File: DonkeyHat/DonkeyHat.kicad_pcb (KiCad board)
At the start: 2 copper layers, 65 x 56.1 mm, 13 parts, among them J1 GPIO, U1 ProMicro

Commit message: WIP
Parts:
- renumbered OLED1 to OLED, Steering1 to Steering, Throttle1 to Throttle
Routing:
- net +3V3: track 97.3 -> 96.7 mm
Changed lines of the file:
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@@
 		(descr "Through hole straight pin header, 1x03, 2.54mm pitch, single row")
 		(tags "Through hole pin header THT 1x03 2.54mm single row")
-		(property "Reference" "Steering1"
+		(property "Reference" "Steering"
 			(at -2.54 2.54 90)
 			(layer "F.SilkS")
@@
 		(descr "Through hole straight socket strip, 1x04, 2.54mm pitch, single row (from Kicad 4.0.7), script generated")
 		(tags "Through hole socket strip THT 1x04 2.54mm single row")
-		(property "Reference" "OLED1"
+		(property "Reference" "OLED"
 			(at 0 -2.77 0)
 			(layer "F.SilkS")
@@
 		(descr "Through hole straight pin header, 1x03, 2.54mm pitch, single row")
 		(tags "Through hole pin header THT 1x03 2.54mm single row")
-		(property "Reference" "Throttle1"
+		(property "Reference" "Throttle"
 			(at 2.54 2.54 270)
 			(layer "F.SilkS")
@@
 	)
 	(segment
-		(start 104.064 64.948)
-		(end 103.81 65.202)
-		(width 0.2)
-		(layer "B.Cu")
-		(net 6)
-	)
-	(segment
-		(start 103.81 65.202)
-		(end 103.81 69.52)
+		(start 101.778 62.662)
+		(end 103.81 64.694)
 		(width 0.2)
 		(layer "B.Cu")
@@
 	)
 	(segment
-		(start 101.778 62.662)
-		(end 104.064 64.948)
+		(start 101.778 61.138)
+		(end 101.778 62.662)
 		(width 0.2)
 		(layer "B.Cu")
@@
 	)
 	(segment
-		(start 101.778 61.138)
-		(end 101.778 62.662)
+		(start 103.81 64.694)
+		(end 103.81 69.52)
 		(width 0.2)
 		(layer "B.Cu")
@@
 	)
 	(segment
-		(start 102.413 66.218)
-		(end 101.397 67.234)
-		(width 0.2)
-		(layer "B.Cu")
-		(net 31)
-	)
-	(segment
-		(start 101.397 67.488)
-		(end 102.159 68.25)
+		(start 102.159 66.472)
+		(end 102.159 86.03)
 		(width 0.2)
 		(layer "B.Cu")
@@
 	)
 	(segment
-		(start 101.397 67.234)
-		(end 101.397 67.488)
-		(width 0.2)
-		(layer "B.Cu")
-		(net 31)
-	)
-	(segment
 		(start 102.413 64.821)
 		(end 102.413 66.218)
@@
 	)
 	(segment
-		(start 102.159 68.25)
-		(end 102.159 86.03)
+		(start 102.413 66.218)
+		(end 102.159 66.472)
 		(width 0.2)
 		(layer "B.Cu")

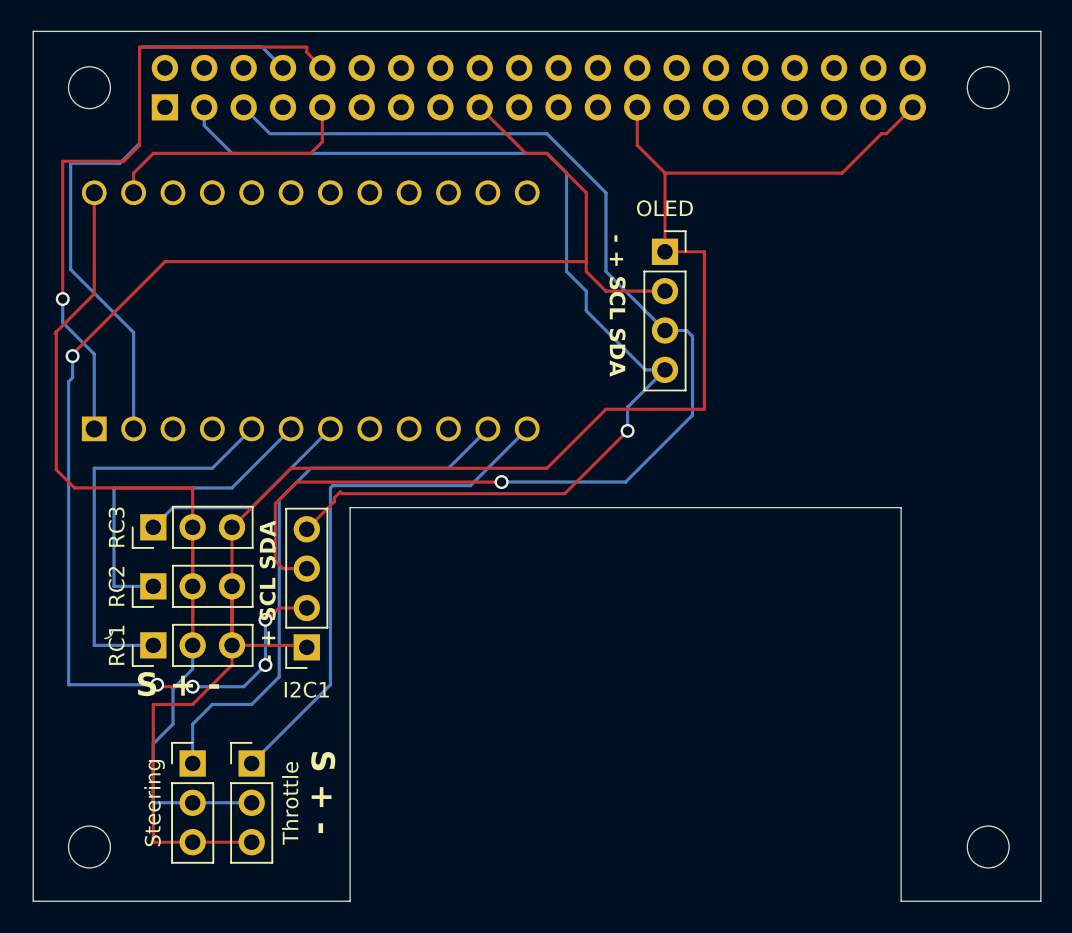
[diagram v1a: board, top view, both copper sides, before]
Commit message: Switched to smaller 2040
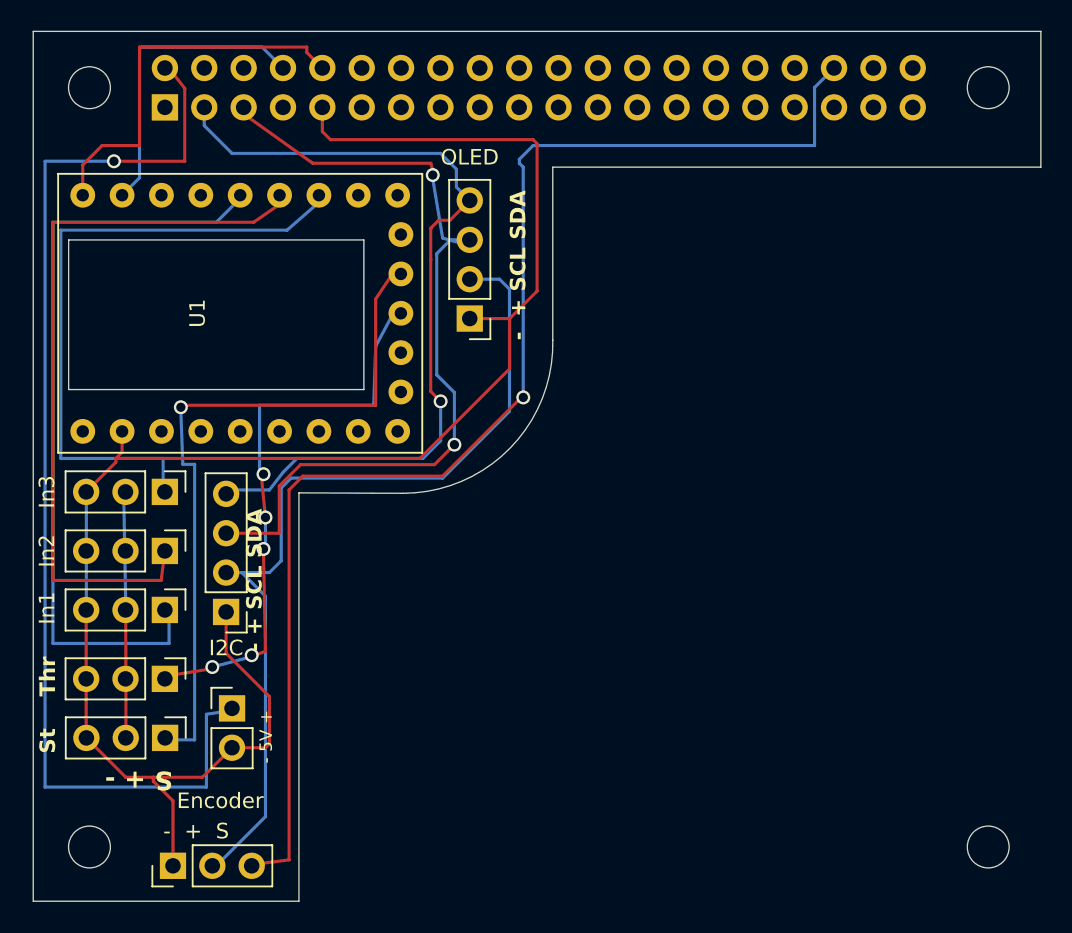
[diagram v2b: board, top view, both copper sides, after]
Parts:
- added Encoder: Conn_01x03_Pin, Connector_PinHeader_2.54mm:PinHeader_1x03_P2.54mm_Vertical, F.Cu at (108.9, 97.7)
- added J2: Conn_01x02_Pin, Connector_PinHeader_2.54mm:PinHeader_1x02_P2.54mm_Vertical, F.Cu at (112.7, 87.6)
- I2C: renamed from I2C1; footprint Connector_PinSocket_2.54mm:PinSocket_1x04_P2.54mm_Vertical -> Connector_PinHeader_2.54mm:PinHeader_1x04_P2.54mm_Vertical
- OLED: footprint Connector_PinSocket_2.54mm:PinSocket_1x04_P2.54mm_Vertical -> Connector_PinHeader_2.54mm:PinHeader_1x04_P2.54mm_Vertical
- U1: footprint promicro:ProMicro-NoSilk -> RP2040-Zero:RP2040-Zero
- moved OLED 13.3 mm to (128.0, 62.4), turned to 180 degrees
- moved U1 11.6 mm to (125.0, 71.1), turned to 90 degrees
- moved Thr1 7.82 mm to (108.4, 85.6), turned to -90 degrees
- moved I2C 5.69 mm to (112.3, 81.3)
- moved St1 2.43 mm to (108.4, 89.5), turned to -90 degrees
- moved In1 2.40 mm to (108.4, 81.2), turned to -90 degrees
- moved In2 2.40 mm to (108.4, 77.4), turned to -90 degrees
- moved In3 2.40 mm to (108.4, 73.6), turned to -90 degrees
- renumbered RC1 to In1, RC2 to In2, RC3 to In3, Steering to St1, Throttle to Thr1
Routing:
- net +BATT: track 62.4 -> 0.02 mm
- net /GPIO3/SCL1: track 78.5 -> 34.2 mm, vias 1 -> 2
- net /GPIO16: track 0.00 -> 40.7 mm, vias 0 -> 1
- net +3V3: track 96.7 -> 57.3 mm, vias 5 -> 0
- net Net-(St1-Pin_1): track 36.2 -> 0.00 mm, vias 0 -> 1
- net Net-(Thr1-Pin_1): track 34.2 -> 0.00 mm, vias 0 -> 5
- net GND: track 132.1 -> 104.4 mm
- net Net-(In1-Pin_1): track 26.5 -> 0.00 mm
- net Net-(In2-Pin_1): track 21.9 -> 0.00 mm
- net /GPIO14/TXD0: track 39.8 -> 19.9 mm
- net /GPIO2/SDA1: track 70.4 -> 51.5 mm
- net /GPIO15/RXD0: track 42.5 -> 25.0 mm, vias 1 -> 0
- net Net-(In3-Pin_1): track 14.1 -> 0.00 mm
- net +5V: vias 0 -> 1
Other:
- outline, holes or cut-outs redrawn
- board text added: "- + S"
- board text added: "- 5V +"
- board text added: "St"
- board text added: "Thr"

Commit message: Added 4-bit encoders
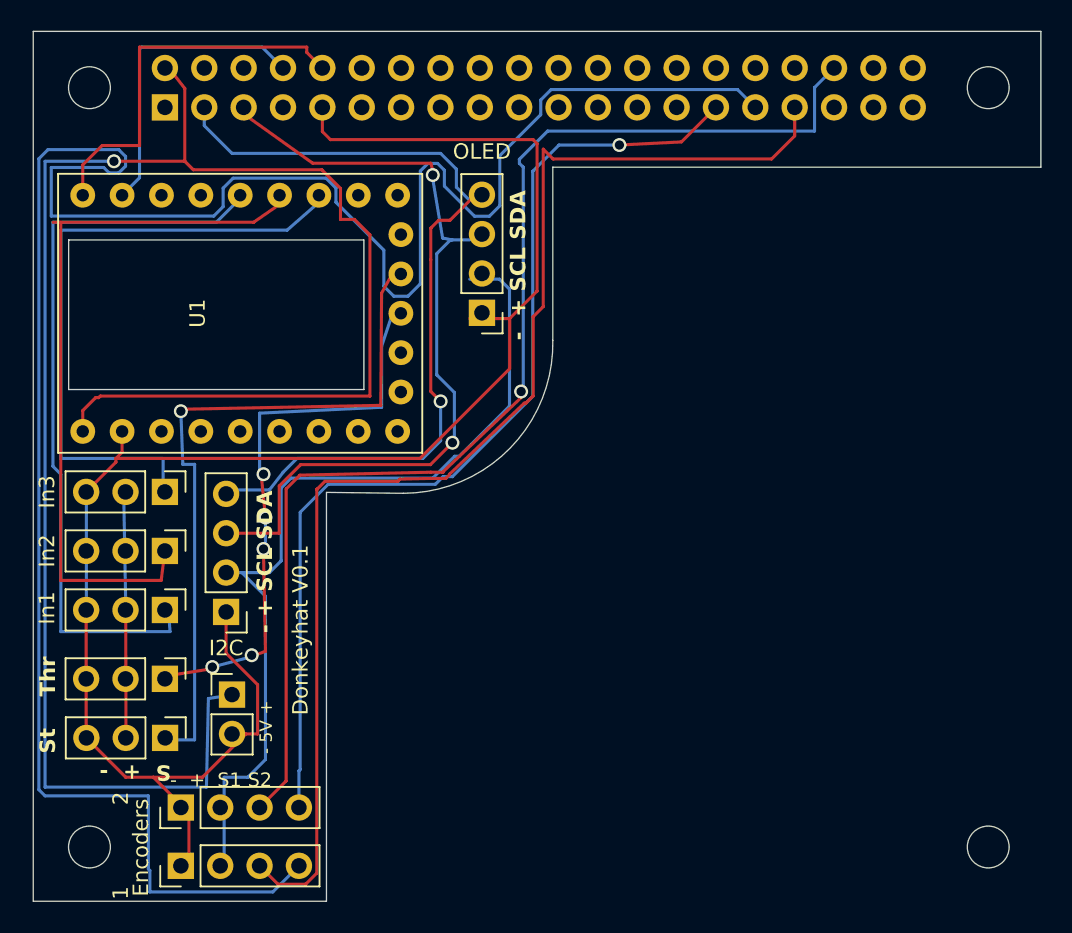
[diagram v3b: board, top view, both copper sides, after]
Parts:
- removed Encoder: Conn_01x03_Pin, Connector_PinHeader_2.54mm:PinHeader_1x03_P2.54mm_Vertical
- added J2: Encoder 2, Connector_PinHeader_2.54mm:PinHeader_1x04_P2.54mm_Vertical, F.Cu at (109.4, 97.7)
- added J3: Encoder 1, Connector_PinHeader_2.54mm:PinHeader_1x04_P2.54mm_Vertical, F.Cu at (109.4, 94.0)
- moved 5V1 0.89 mm to (112.7, 86.7)
- moved OLED 0.87 mm to (128.8, 62.0)
- renumbered J2 to 5V1
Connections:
- U1 pad 22: unconnected-(U1-RST-Pad22) -> +5V
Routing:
- net /GPIO6: track 0.00 -> 147.8 mm
- net /GPIO13/PWM1: track 0.00 -> 80.8 mm
- net /GPIO5: track 0.00 -> 65.4 mm, vias 0 -> 1
- net +5V: track 0.00 -> 45.8 mm
- net /GPIO16: track 40.7 -> 61.8 mm
- net Net-(In1-Pin_1): track 0.00 -> 10.9 mm
- net GND: track 104.4 -> 103.4 mm
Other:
- outline, holes or cut-outs redrawn
- board text added: "- + S1 S2"
- board text added: "1"
- board text added: "2"
- board text added: "Donkeyhat V0.1"
- board text added: "Encoders"
- board text removed: "- + S"

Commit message: Switched encoders to RP2040
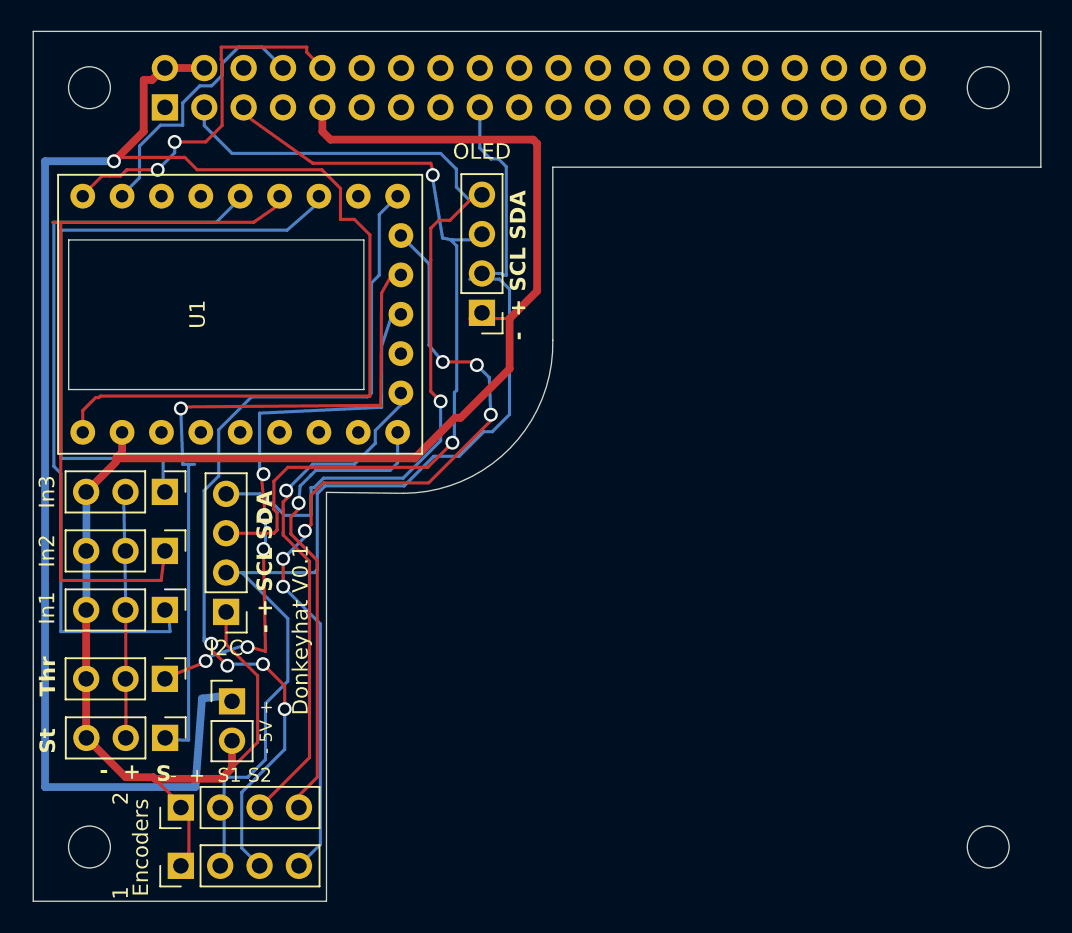
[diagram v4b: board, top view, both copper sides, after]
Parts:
- moved 5V1 0.43 mm to (112.7, 87.1)
- moved U1 0.06 mm to (125.0, 71.1)
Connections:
- J1 pad 31: /GPIO6 -> unconnected-(J1-Pin_31-Pad31)
- J2 pad 3: /GPIO13/PWM1 -> Net-(J2-Pin_3)
- J2 pad 4: /GPIO6 -> Net-(J2-Pin_4)
- J3 pad 3: /GPIO16 -> Net-(J3-Pin_3)
- J3 pad 4: /GPIO5 -> Net-(J3-Pin_4)
- U1 pad 10: unconnected-(U1-E6-Pad10) -> Net-(J2-Pin_4)
- U1 pad 14: unconnected-(U1-B2-Pad14) -> Net-(J3-Pin_3)
- U1 pad 15: unconnected-(U1-B3-Pad15) -> Net-(J3-Pin_4)
- U1 pad 9: unconnected-(U1-D7-Pad9) -> Net-(J2-Pin_3)
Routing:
- net /GPIO6: track 147.8 -> 0.00 mm
- net /GPIO13/PWM1: track 80.8 -> 0.00 mm
- net /GPIO5: track 65.4 -> 0.00 mm, vias 1 -> 0
- net /GPIO16: track 61.8 -> 0.00 mm, vias 1 -> 0
- net Net-(J2-Pin_3): track 0.00 -> 59.1 mm, vias 0 -> 4
- net Net-(J2-Pin_4): track 0.00 -> 56.5 mm, vias 0 -> 6
- net Net-(J3-Pin_3): track 0.00 -> 34.1 mm, vias 0 -> 1
- net Net-(J3-Pin_4): track 0.00 -> 31.2 mm, vias 0 -> 1
- net +3V3: track 57.8 -> 72.9 mm
- net +5V: track 45.8 -> 56.1 mm
- net /GPIO2/SDA1: track 51.5 -> 55.7 mm
- net GND: track 103.4 -> 106.0 mm
- net /GPIO14/TXD0: track 19.9 -> 17.6 mm
- net /GPIO15/RXD0: track 25.0 -> 23.9 mm, vias 0 -> 2

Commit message: tweaks
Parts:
- U1: footprint RP2040-Zero:RP2040-Zero -> RP2040-Zero:RP2040-Zero-bigholes

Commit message: production version
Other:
- board text added: "+ S1 S2"
- board text added: "Donkeyhat V0.2"
- board text added: "I2C + SCL SDA"
- board text removed: "- + S1 S2"
- board text removed: "1"
- board text removed: "2"
- board text removed: "Donkeyhat V0.1"
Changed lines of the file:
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@@
 		(tags "Through hole pin header THT 1x04 2.54mm single row")
 		(property "Reference" "J2"
-			(at 0 -2.33 270)
+			(at 0 -2.33 -90)
 			(layer "F.SilkS")
 			(hide yes)
@@
 		)
 		(property "Value" "Encoder 2"
-			(at 0 9.949999 270)
+			(at 0 9.949999 -90)
 			(layer "F.Fab")
 			(hide yes)
@@
 		(tags "Through hole pin header THT 1x04 2.54mm single row")
 		(property "Reference" "J3"
-			(at 0 -2.33 270)
+			(at 0 -2.33 -90)
 			(layer "F.SilkS")
 			(hide yes)
@@
 		)
 		(property "Value" "Encoder 1"
-			(at 0 9.949999 270)
+			(at 0 9.949999 -90)
 			(layer "F.Fab")
 			(hide yes)
@@
 		(tags "Through hole pin header THT 1x04 2.54mm single row")
 		(property "Reference" "I2C"
-			(at 0 -2.33 180)
+			(at -2.681 -1.469 90)
 			(layer "F.SilkS")
+			(hide yes)
 			(effects
 				(font
@@
 		(layer "Edge.Cuts")
 	)
-	(gr_text "2"
-		(at 106.1 93.8 90)
-		(layer "F.SilkS")
-		(effects
-			(font
-				(size 1 1)
-				(thickness 0.15)
-			)
-			(justify left bottom)
-		)
-	)
 	(gr_text "Thr"
 		(at 101.397 86.792 90)
@@
 		)
 	)
-	(gr_text "- + SCL SDA"
-		(at 115.4 82.7 90)
+	(gr_text "I2C + SCL SDA"
+		(at 114.8 83.7 90)
 		(layer "F.SilkS")
 		(effects
@@
 		)
 	)
-	(gr_text "-  +  S1 S2"
-		(at 108.7 92.4 0)
+	(gr_text "   +  S1 S2"
+		(at 109.1 92.4 0)
 		(layer "F.SilkS")
 		(effects
@@
 			(font
 				(size 1 1)
-				(thickness 0.2)
+				(thickness 0.25)
 				(bold yes)
 			)
@@
 		)
 	)
-	(gr_text "1"
-		(at 106.1 99.9 90)
-		(layer "F.SilkS")
-		(effects
-			(font
-				(size 1 1)
-				(thickness 0.15)
-			)
-			(justify left bottom)
-		)
-	)
 	(gr_text "- 5V +"
 		(at 115.367 90.5 90)
@@
 		)
 	)
-	(gr_text "Donkeyhat V0.1"
+	(gr_text "Donkeyhat V0.2"
 		(at 117.7 88 90)
 		(layer "F.SilkS")
